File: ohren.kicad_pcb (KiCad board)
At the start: 2 copper layers, 60 x 28.7 mm, 35 parts, among them J1 Conn_01x19_MountingPin, U1 TLC5955RTQ

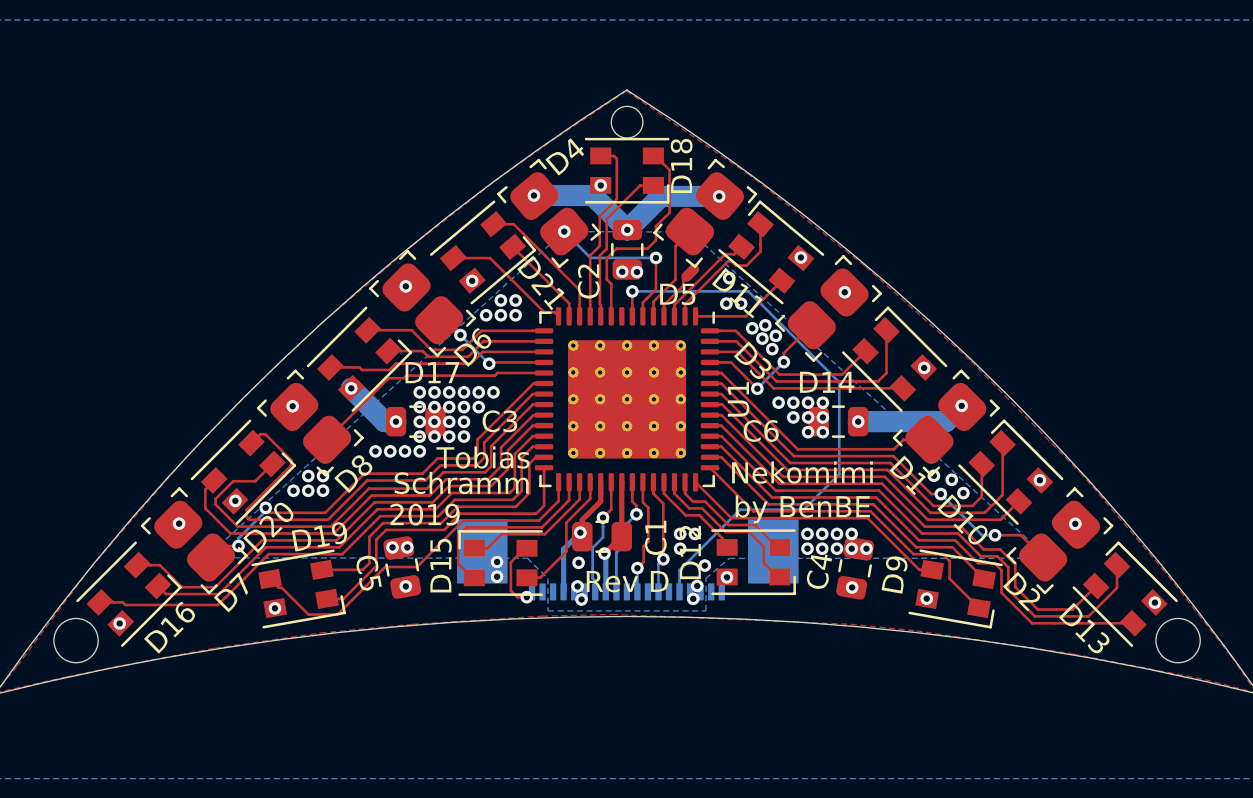
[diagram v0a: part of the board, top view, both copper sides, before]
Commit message: Use custom LED footprint with associated 3D model
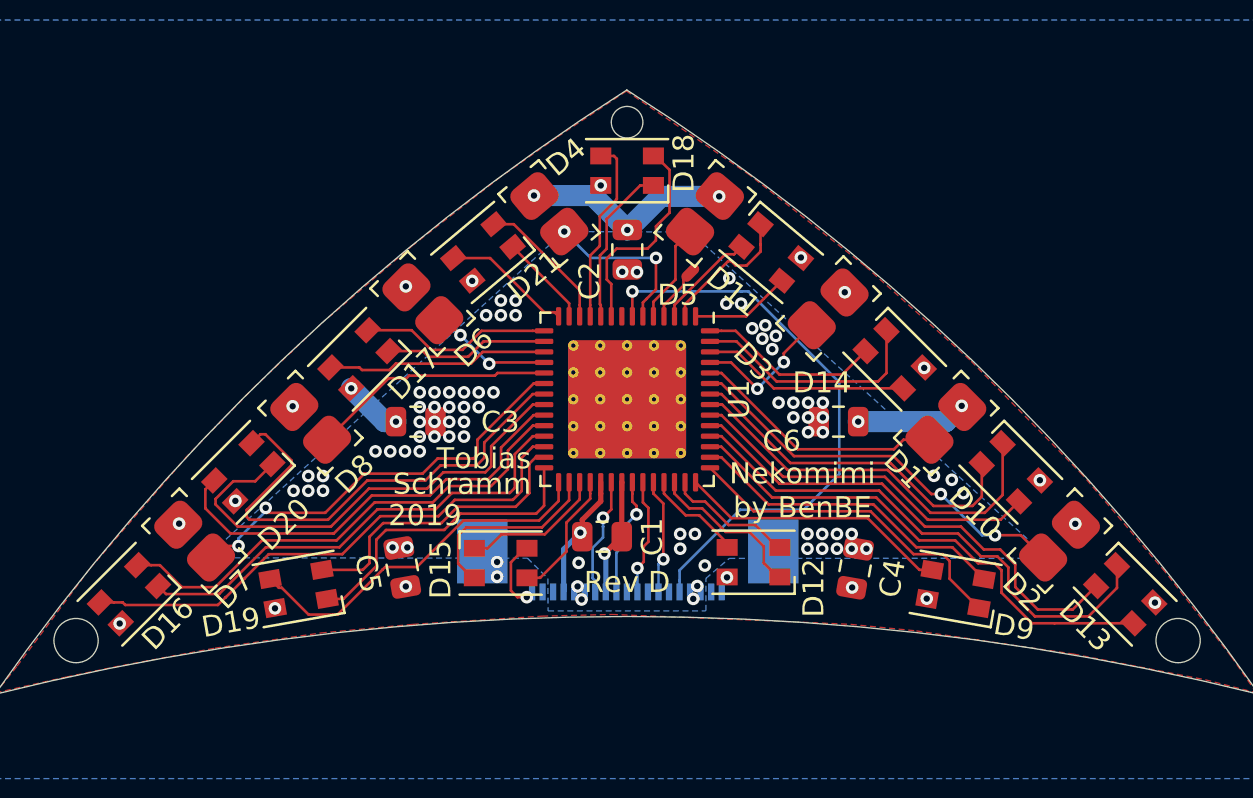
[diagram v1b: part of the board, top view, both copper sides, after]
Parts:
- D10, D11, D12, D13, D14, D15, D16, D17, D18, D19, D20, D21, D9: footprint LED_SMD:LED_Cree-PLCC4_3.2x2.8mm_CCW -> catear-pcb:ASMB-MTB1-0A3A2

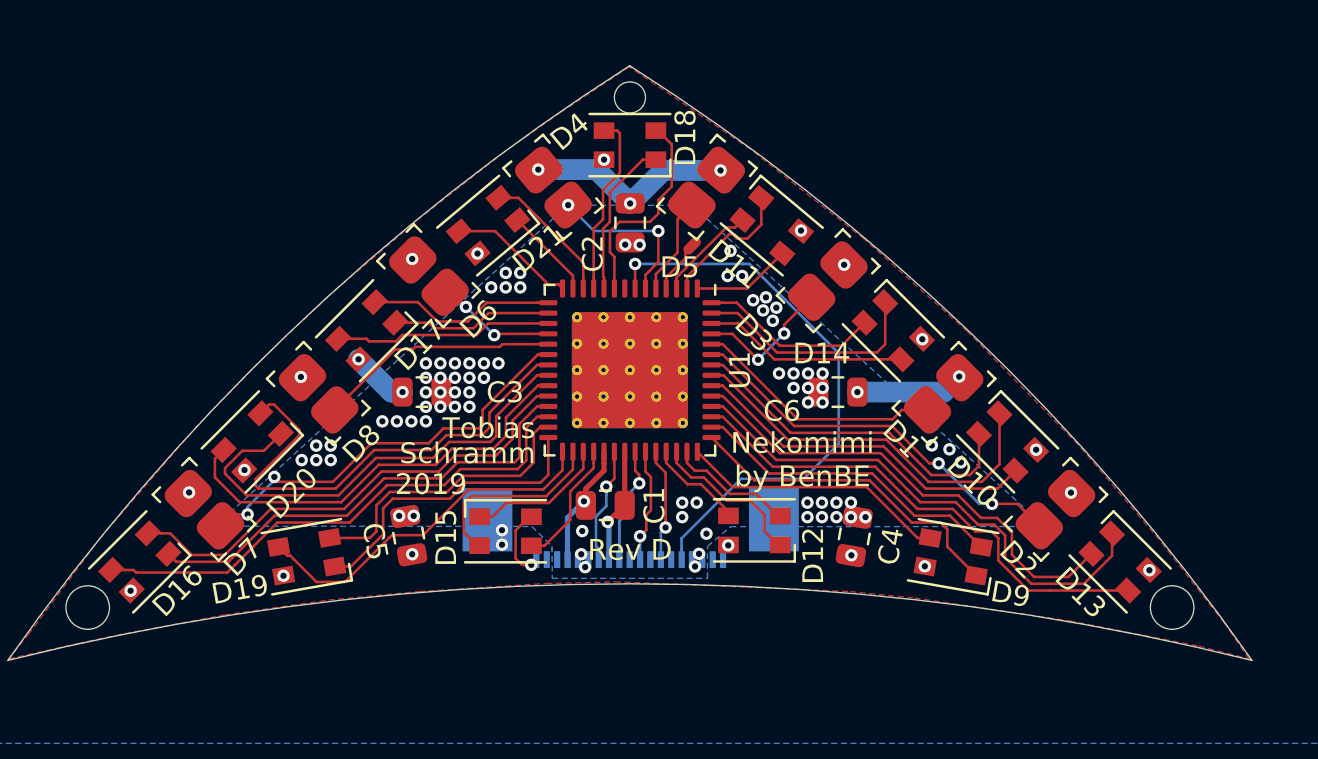
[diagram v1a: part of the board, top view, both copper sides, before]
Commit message: Fix RGB LED routing
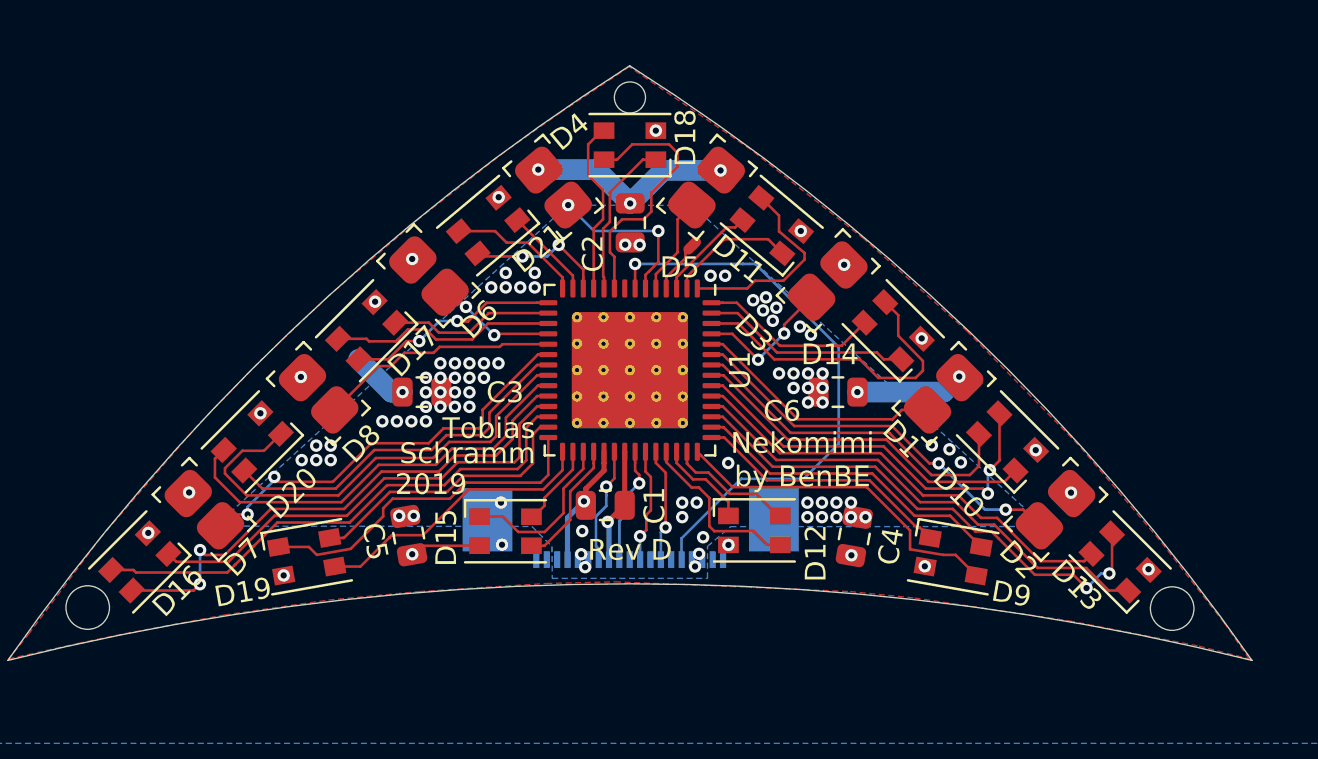
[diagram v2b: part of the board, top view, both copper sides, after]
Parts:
- turned D10 to 135 degrees
- turned D11 to 140 degrees
- turned D12 to 0 degrees
- turned D13 to 135 degrees
- turned D14 to 135 degrees
- turned D19 to 10 degrees
- turned D9 to 350 degrees
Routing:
- net /U1_B6: track 9.87 -> 15.5 mm
- net /U1_G13: track 23.2 -> 17.9 mm
- net /U1_G8: track 9.19 -> 4.02 mm
- net /U1_B3: track 4.80 -> 9.65 mm
- net /U1_B4: track 4.72 -> 8.45 mm
- net /U1_B12: track 17.5 -> 13.8 mm
- net /U1_R0: track 16.0 -> 12.6 mm
- net /U1_B0: track 13.0 -> 16.4 mm
- net /U1_R4: track 7.63 -> 4.49 mm
- net /U1_G11: track 10.2 -> 12.8 mm
- net /U1_B1: track 17.1 -> 19.6 mm, vias 0 -> 2
- net /U1_G9: track 23.4 -> 25.6 mm, vias 0 -> 2
- net /U1_R12: track 14.7 -> 16.7 mm
- net /U1_R1: track 18.8 -> 17.0 mm
- net /U1_R5: track 25.1 -> 23.8 mm
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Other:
- net class Default: clearance 0.2 -> 0.127
- rule trace_clearance: 0.2 -> 0.127

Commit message: RevE
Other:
- board text added: "Rev E"
- board text removed: "Rev D"
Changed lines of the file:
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@@
     (effects (font (size 1 1) (thickness 0.15)))
   )
-  (gr_text "Rev D" (at 140 110.68) (layer F.SilkS)
+  (gr_text "Rev E" (at 140 110.68) (layer F.SilkS)
     (effects (font (size 1 1) (thickness 0.15)))
   )

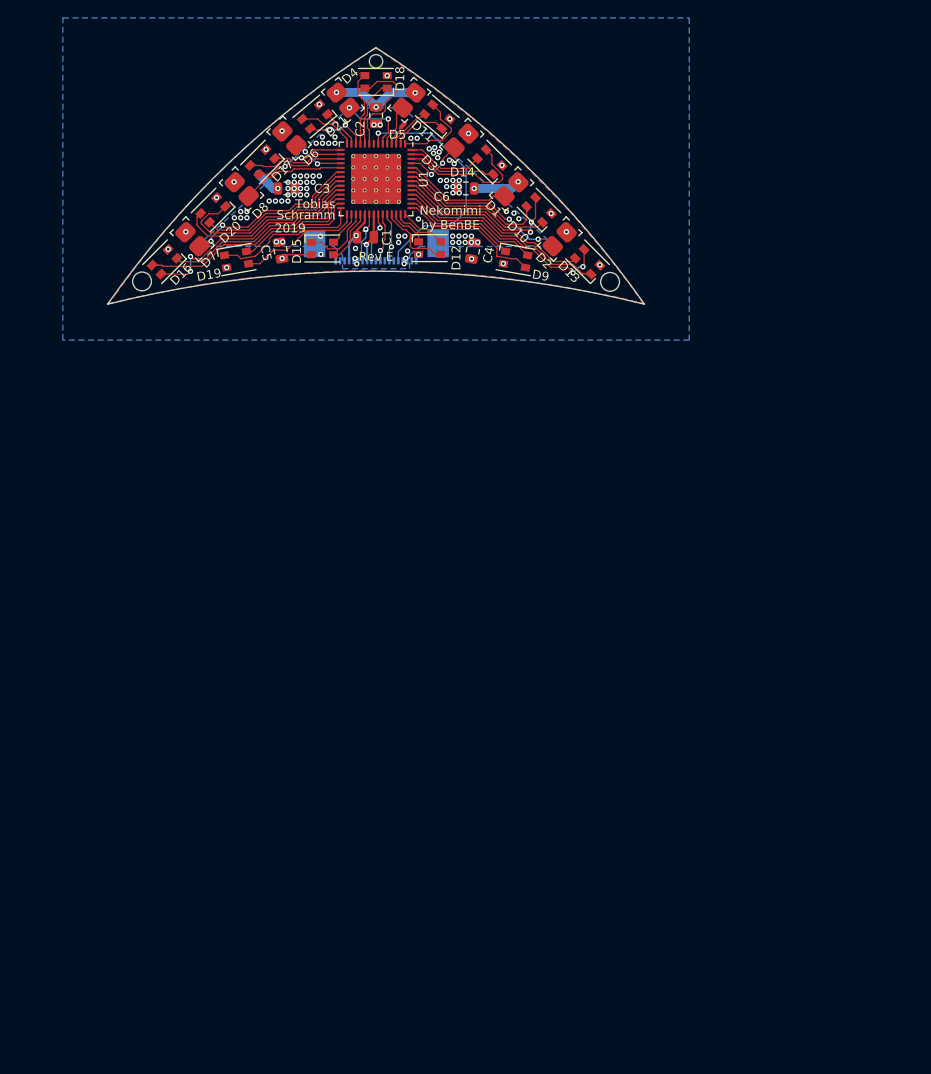
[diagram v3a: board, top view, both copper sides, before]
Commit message: Convert to panelizeable PCB
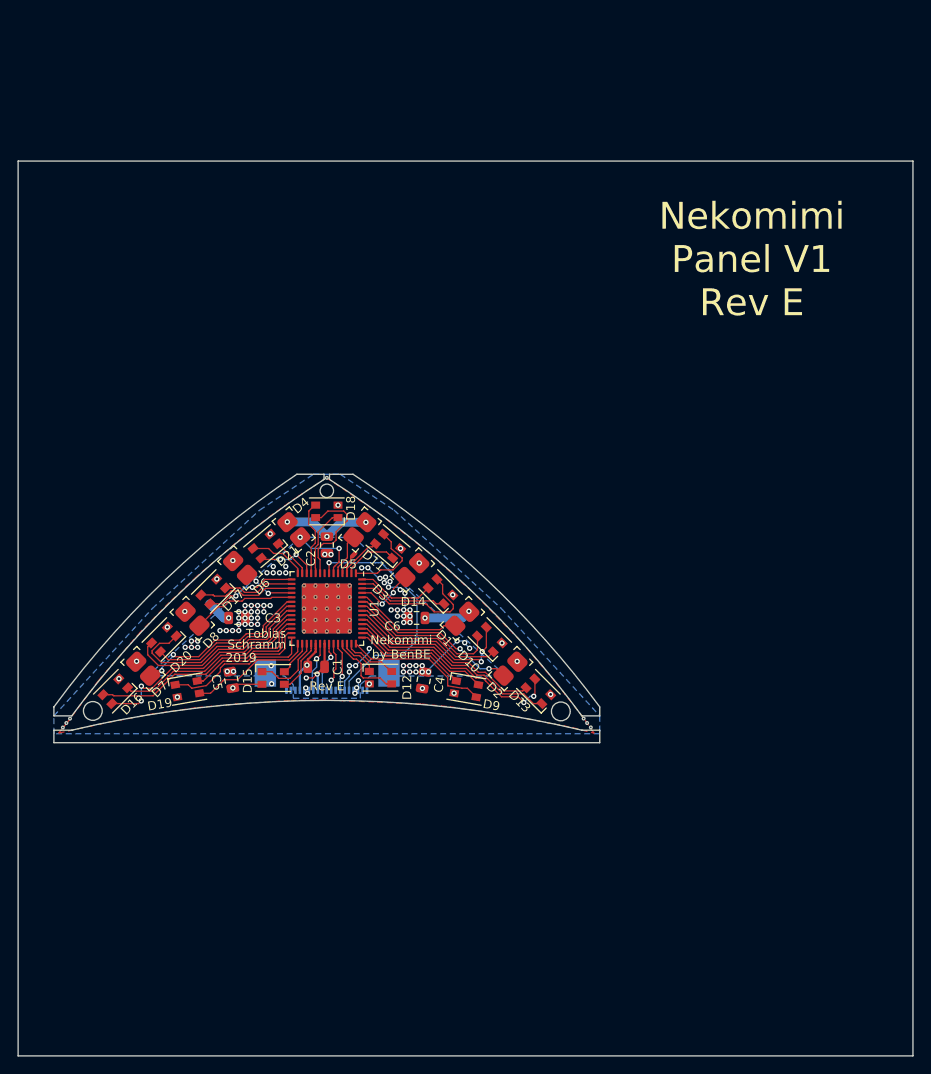
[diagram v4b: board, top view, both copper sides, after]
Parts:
- removed the REF** at (166.2, 113.5)
- removed the REF** at (113.8, 113.5)
- added REF**: npth_0.3, catear-pcb:npth_0.3, B.Cu at (105.0, 163.3)
- added REF**: MountingHole_2.1mm, MountingHole:MountingHole_2.1mm, F.Cu at (160.7, 161.5)
- added REF**: npth_0.3, catear-pcb:npth_0.3, B.Cu at (105.4, 162.8)
- added REF**: npth_0.3, catear-pcb:npth_0.3, B.Cu at (105.8, 162.3)
- added REF**: npth_0.3, catear-pcb:npth_0.3, F.Cu at (134.5, 135.4)
- added REF**: npth_0.3, catear-pcb:npth_0.3, F.Cu at (164.0, 163.3)
- added REF**: npth_0.3, catear-pcb:npth_0.3, F.Cu at (163.6, 162.8)
- added REF**: npth_0.3, catear-pcb:npth_0.3, F.Cu at (163.2, 162.3)
- added REF**: MountingHole_2.1mm, MountingHole:MountingHole_2.1mm, F.Cu at (108.3, 161.4)
- moved G*** 48.8 mm to (117.0, 159.0)
- moved G*** 48.4 mm to (149.5, 155.0)
- moved C1 48.3 mm to (133.3, 156.5)
- moved C4 48.3 mm to (145.3, 158.0)
- moved D15 48.3 mm to (128.5, 157.8)
- moved C2 48.3 mm to (134.5, 142.9)
- moved C3 48.3 mm to (124.5, 151.1)
- moved C6 48.3 mm to (144.5, 151.1)
- moved D1 48.3 mm to (149.6, 151.1)
- moved D10 48.3 mm to (152.7, 153.5)
- moved D11 48.3 mm to (141.3, 143.0)
- moved D13 48.3 mm to (158.1, 159.2)
- moved D14 48.3 mm to (147.2, 148.1)
- moved D16 48.3 mm to (110.9, 159.2)
- moved D17 48.3 mm to (121.8, 148.1)
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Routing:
- net GND: track 5.61 -> 61.3 mm
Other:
- board size 60 x 28.7 mm -> 100 x 100 mm
- board text added: "Nekomimi Panel V1 Rev E"

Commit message: Finish panel
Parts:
- added C1: C, Capacitor_SMD:C_0805_2012Metric, F.Cu at (175.5, 148.8)
- added C1: C, Capacitor_SMD:C_0805_2012Metric, F.Cu at (135.7, 175.0)
- added C1: C, Capacitor_SMD:C_0805_2012Metric, F.Cu at (133.3, 124.5)
- added C2: C, Capacitor_SMD:C_0805_2012Metric, F.Cu at (189.1, 150.0)
- added C2: C, Capacitor_SMD:C_0805_2012Metric, F.Cu at (134.5, 188.6)
- added C2: C, Capacitor_SMD:C_0805_2012Metric, F.Cu at (134.5, 110.9)
- added C3: C, Capacitor_SMD:C_0805_2012Metric, F.Cu at (180.9, 140.0)
- added C3: C, Capacitor_SMD:C_0805_2012Metric, F.Cu at (144.5, 180.4)
- added C3: C, Capacitor_SMD:C_0805_2012Metric, F.Cu at (124.5, 119.1)
- added C4: C, Capacitor_SMD:C_0805_2012Metric, F.Cu at (174.0, 160.8)
- added C4: C, Capacitor_SMD:C_0805_2012Metric, F.Cu at (123.7, 173.5)
- added C4: C, Capacitor_SMD:C_0805_2012Metric, F.Cu at (145.3, 126.0)
- added C5: C, Capacitor_SMD:C_0805_2012Metric, F.Cu at (174.0, 139.3)
- added C5: C, Capacitor_SMD:C_0805_2012Metric, F.Cu at (145.2, 173.5)
- added C5: C, Capacitor_SMD:C_0805_2012Metric, F.Cu at (123.8, 126.0)
- added C6: C, Capacitor_SMD:C_0805_2012Metric, F.Cu at (180.9, 160.0)
- added C6: C, Capacitor_SMD:C_0805_2012Metric, F.Cu at (124.5, 180.4)
- added C6: C, Capacitor_SMD:C_0805_2012Metric, F.Cu at (144.5, 119.1)
- added D1: LED, catear-pcb:smd_led_universal, F.Cu at (180.9, 165.1)
- added D1: LED, catear-pcb:smd_led_universal, F.Cu at (119.4, 180.4)
- added D1: LED, catear-pcb:smd_led_universal, F.Cu at (149.6, 119.1)
- added D10: LED_ARGB, catear-pcb:ASMB-MTB1-0A3A2, F.Cu at (178.5, 168.2)
- added D10: LED_ARGB, catear-pcb:ASMB-MTB1-0A3A2, F.Cu at (116.3, 178.0)
- added D10: LED_ARGB, catear-pcb:ASMB-MTB1-0A3A2, F.Cu at (152.7, 121.5)
- added D11: LED_ARGB, catear-pcb:ASMB-MTB1-0A3A2, F.Cu at (189.0, 156.8)
- added D11: LED_ARGB, catear-pcb:ASMB-MTB1-0A3A2, F.Cu at (127.7, 188.5)
- added D11: LED_ARGB, catear-pcb:ASMB-MTB1-0A3A2, F.Cu at (141.3, 111.0)
- added D12: LED_ARGB, catear-pcb:ASMB-MTB1-0A3A2, F.Cu at (174.3, 156.0)
- added D12: LED_ARGB, catear-pcb:ASMB-MTB1-0A3A2, F.Cu at (128.5, 173.8)
- added D12: LED_ARGB, catear-pcb:ASMB-MTB1-0A3A2, F.Cu at (140.5, 125.7)
- added D13: LED_ARGB, catear-pcb:ASMB-MTB1-0A3A2, F.Cu at (172.8, 173.6)
- added D13: LED_ARGB, catear-pcb:ASMB-MTB1-0A3A2, F.Cu at (110.9, 172.2)
- added D13: LED_ARGB, catear-pcb:ASMB-MTB1-0A3A2, F.Cu at (158.1, 127.2)
- added D14: LED_ARGB, catear-pcb:ASMB-MTB1-0A3A2, F.Cu at (183.9, 162.7)
- added D14: LED_ARGB, catear-pcb:ASMB-MTB1-0A3A2, F.Cu at (121.8, 183.4)
- added D14: LED_ARGB, catear-pcb:ASMB-MTB1-0A3A2, F.Cu at (147.2, 116.1)
- added D15: LED_ARGB, catear-pcb:ASMB-MTB1-0A3A2, F.Cu at (174.2, 144.0)
- added D15: LED_ARGB, catear-pcb:ASMB-MTB1-0A3A2, F.Cu at (140.5, 173.7)
- added D15: LED_ARGB, catear-pcb:ASMB-MTB1-0A3A2, F.Cu at (128.5, 125.8)
- added D16: LED_ARGB, catear-pcb:ASMB-MTB1-0A3A2, F.Cu at (172.8, 126.4)
- added D16: LED_ARGB, catear-pcb:ASMB-MTB1-0A3A2, F.Cu at (158.1, 172.2)
- added D16: LED_ARGB, catear-pcb:ASMB-MTB1-0A3A2, F.Cu at (110.9, 127.2)
- added D17: LED_ARGB, catear-pcb:ASMB-MTB1-0A3A2, F.Cu at (183.9, 137.3)
- added D17: LED_ARGB, catear-pcb:ASMB-MTB1-0A3A2, F.Cu at (147.2, 183.4)
- added D17: LED_ARGB, catear-pcb:ASMB-MTB1-0A3A2, F.Cu at (121.8, 116.1)
- added D18: LED_ARGB, catear-pcb:ASMB-MTB1-0A3A2, F.Cu at (192.8, 150.0)
- added D18: LED_ARGB, catear-pcb:ASMB-MTB1-0A3A2, F.Cu at (134.5, 192.3)
- added D18: LED_ARGB, catear-pcb:ASMB-MTB1-0A3A2, F.Cu at (134.5, 107.2)
- added D19: LED_ARGB, catear-pcb:ASMB-MTB1-0A3A2, F.Cu at (173.0, 134.4)
- added D19: LED_ARGB, catear-pcb:ASMB-MTB1-0A3A2, F.Cu at (150.1, 172.5)
- added D19: LED_ARGB, catear-pcb:ASMB-MTB1-0A3A2, F.Cu at (118.9, 127.0)
- added D2: LED, catear-pcb:smd_led_universal, F.Cu at (175.3, 170.5)
- added D2: LED, catear-pcb:smd_led_universal, F.Cu at (114.0, 174.8)
- added D2: LED, catear-pcb:smd_led_universal, F.Cu at (155.0, 124.7)
- added D20: LED_ARGB, catear-pcb:ASMB-MTB1-0A3A2, F.Cu at (178.5, 131.8)
- added D20: LED_ARGB, catear-pcb:ASMB-MTB1-0A3A2, F.Cu at (152.7, 178.0)
- added D20: LED_ARGB, catear-pcb:ASMB-MTB1-0A3A2, F.Cu at (116.3, 121.5)
- added D21: LED_ARGB, catear-pcb:ASMB-MTB1-0A3A2, F.Cu at (189.0, 143.2)
- added D21: LED_ARGB, catear-pcb:ASMB-MTB1-0A3A2, F.Cu at (141.3, 188.5)
- added D21: LED_ARGB, catear-pcb:ASMB-MTB1-0A3A2, F.Cu at (127.7, 111.0)
- added D3: LED, catear-pcb:smd_led_universal, F.Cu at (186.3, 159.6)
- added D3: LED, catear-pcb:smd_led_universal, F.Cu at (124.9, 185.8)
- added D3: LED, catear-pcb:smd_led_universal, F.Cu at (144.1, 113.7)
- added D4: LED, catear-pcb:smd_led_universal, F.Cu at (190.8, 146.3)
- added D4: LED, catear-pcb:smd_led_universal, F.Cu at (138.2, 190.3)
- added D4: LED, catear-pcb:smd_led_universal, F.Cu at (130.8, 109.2)
- added D5: LED, catear-pcb:smd_led_universal, F.Cu at (190.8, 153.7)
- added D5: LED, catear-pcb:smd_led_universal, F.Cu at (130.8, 190.3)
- added D5: LED, catear-pcb:smd_led_universal, F.Cu at (138.2, 109.2)
- added D6: LED, catear-pcb:smd_led_universal, F.Cu at (186.6, 140.3)
- added D6: LED, catear-pcb:smd_led_universal, F.Cu at (144.2, 186.1)
- added D6: LED, catear-pcb:smd_led_universal, F.Cu at (124.8, 113.5)
- added D7: LED, catear-pcb:smd_led_universal, F.Cu at (175.3, 129.5)
- added D7: LED, catear-pcb:smd_led_universal, F.Cu at (155.0, 174.8)
- added D7: LED, catear-pcb:smd_led_universal, F.Cu at (114.0, 124.7)
- added D8: LED, catear-pcb:smd_led_universal, F.Cu at (180.9, 135.0)
- added D8: LED, catear-pcb:smd_led_universal, F.Cu at (149.5, 180.4)
- added D8: LED, catear-pcb:smd_led_universal, F.Cu at (119.5, 119.1)
- added D9: LED_ARGB, catear-pcb:ASMB-MTB1-0A3A2, F.Cu at (173.0, 165.6)
- added D9: LED_ARGB, catear-pcb:ASMB-MTB1-0A3A2, F.Cu at (118.9, 172.5)
- added D9: LED_ARGB, catear-pcb:ASMB-MTB1-0A3A2, F.Cu at (150.1, 127.0)
- added G***: LOGO, catear-pcb:attribution, B.Cu at (173.0, 132.5)
- added G***: LOGO, catear-pcb:catboy, B.Cu at (177.0, 165.0)
- added G***: LOGO, catear-pcb:attribution, B.Cu at (152.0, 172.5)
- added G***: LOGO, catear-pcb:catboy, B.Cu at (119.5, 176.5)
- added G***: LOGO, catear-pcb:attribution, B.Cu at (117.0, 127.0)
- added G***: LOGO, catear-pcb:catboy, B.Cu at (149.5, 123.0)
- added J1: Conn_01x19_MountingPin, catear-pcb:Molex_Easy-On_52746-1971_1x19_P0.5mm_Horizontal, B.Cu at (172.9, 150.0)
- added J1: Conn_01x19_MountingPin, catear-pcb:Molex_Easy-On_52746-1971_1x19_P0.5mm_Horizontal, B.Cu at (134.5, 172.4)
- added J1: Conn_01x19_MountingPin, catear-pcb:Molex_Easy-On_52746-1971_1x19_P0.5mm_Horizontal, B.Cu at (134.5, 127.1)
- added REF**: MountingHole_3.2mm_M3, MountingHole:MountingHole_3.2mm_M3, F.Cu at (160.0, 140.0)
- added REF**: npth_0.3, catear-pcb:npth_0.3, F.Cu at (169.2, 179.1)
- added REF**: npth_0.3, catear-pcb:npth_0.3, F.Cu at (168.7, 179.5)
- added REF**: npth_0.3, catear-pcb:npth_0.3, B.Cu at (169.7, 121.3)
- added REF**: MountingHole_2.1mm, MountingHole:MountingHole_2.1mm, F.Cu at (170.6, 123.8)
- added REF**: MountingHole_1.5mm, catear-pcb:MountingHole_1mm, F.Cu at (195.2, 150.0)
- added REF**: MountingHole_2.1mm, MountingHole:MountingHole_2.1mm, F.Cu at (170.5, 176.2)
- added REF**: npth_0.3, catear-pcb:npth_0.3, F.Cu at (134.5, 196.1)
- added REF**: npth_0.3, catear-pcb:npth_0.3, B.Cu at (164.0, 168.2)
- added REF**: npth_0.3, catear-pcb:npth_0.3, B.Cu at (163.6, 168.7)
- added REF**: npth_0.3, catear-pcb:npth_0.3, F.Cu at (105.8, 169.2)
- added REF**: MountingHole_3.2mm_M3, MountingHole:MountingHole_3.2mm_M3, F.Cu at (195.0, 195.0)
- added REF**: npth_0.3, catear-pcb:npth_0.3, F.Cu at (105.4, 168.7)
- added REF**: npth_0.3, catear-pcb:npth_0.3, F.Cu at (105.0, 168.2)
- added REF**: npth_0.3, catear-pcb:npth_0.3, B.Cu at (163.2, 169.2)
- added REF**: MountingHole_2.1mm, MountingHole:MountingHole_2.1mm, F.Cu at (160.7, 170.1)
- added REF**: MountingHole_1.5mm, catear-pcb:MountingHole_1mm, F.Cu at (134.5, 194.7)
- added REF**: MountingHole_2.1mm, MountingHole:MountingHole_2.1mm, F.Cu at (108.3, 170.0)
- added REF**: npth_0.3, catear-pcb:npth_0.3, F.Cu at (134.5, 103.4)
- added REF**: npth_0.3, catear-pcb:npth_0.3, B.Cu at (105.0, 131.3)
- added REF**: npth_0.3, catear-pcb:npth_0.3, B.Cu at (105.4, 130.8)
- added REF**: npth_0.3, catear-pcb:npth_0.3, F.Cu at (163.2, 130.3)
- added REF**: MountingHole_3.2mm_M3, MountingHole:MountingHole_3.2mm_M3, F.Cu at (105.0, 195.0)
- added REF**: npth_0.3, catear-pcb:npth_0.3, F.Cu at (163.6, 130.8)
- added REF**: npth_0.3, catear-pcb:npth_0.3, F.Cu at (164.0, 131.3)
- added REF**: npth_0.3, catear-pcb:npth_0.3, B.Cu at (105.8, 130.3)
- added REF**: MountingHole_2.1mm, MountingHole:MountingHole_2.1mm, F.Cu at (108.3, 129.4)
- added REF**: MountingHole_1.5mm, catear-pcb:MountingHole_1mm, F.Cu at (134.5, 104.8)
- added REF**: MountingHole_2.1mm, MountingHole:MountingHole_2.1mm, F.Cu at (160.7, 129.5)
- added REF**: MountingHole_3.2mm_M3, MountingHole:MountingHole_3.2mm_M3, F.Cu at (105.0, 105.0)
- added REF**: MountingHole_3.2mm_M3, MountingHole:MountingHole_3.2mm_M3, F.Cu at (195.0, 105.0)
- added REF**: npth_0.3, catear-pcb:npth_0.3, F.Cu at (196.6, 150.0)
- added REF**: npth_0.3, catear-pcb:npth_0.3, B.Cu at (168.7, 120.5)
- added REF**: npth_0.3, catear-pcb:npth_0.3, B.Cu at (169.2, 120.9)
- added REF**: npth_0.3, catear-pcb:npth_0.3, F.Cu at (169.7, 178.7)
- added TP1: TestPoint, catear-pcb:TestPoint_0.5x1mm, F.Cu at (188.0, 153.0)
- added TP1: TestPoint, catear-pcb:TestPoint_0.5x1mm, F.Cu at (131.5, 187.5)
- added TP1: TestPoint, catear-pcb:TestPoint_0.5x1mm, F.Cu at (137.5, 112.0)
- added U1: TLC5955RTQ, Package_DFN_QFN:QFN-56-1EP_8x8mm_P0.5mm_EP5.6x5.6mm_ThermalVias, F.Cu at (182.0, 150.0)
- added U1: TLC5955RTQ, Package_DFN_QFN:QFN-56-1EP_8x8mm_P0.5mm_EP5.6x5.6mm_ThermalVias, F.Cu at (134.5, 181.5)
- added U1: TLC5955RTQ, Package_DFN_QFN:QFN-56-1EP_8x8mm_P0.5mm_EP5.6x5.6mm_ThermalVias, F.Cu at (134.5, 118.0)
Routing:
- net (no net): track 0.00 -> 2235.2 mm, vias 0 -> 393
- added copper zone on B.Cu, net (none)
- added copper zone on F.Cu, net (none)
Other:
- outline, holes or cut-outs redrawn
